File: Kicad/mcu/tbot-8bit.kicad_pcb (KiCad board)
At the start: 2 copper layers, 80 x 100 mm, 69 parts, among them IC201 TLV1117-50, IC301 PIC16F1778, IC401 MCP2221A, K201 Battery, K301 MCU 1, K302 ICSP, K303 MCU 2, K401 VIN, K402 FRONT #1, K403 +5V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

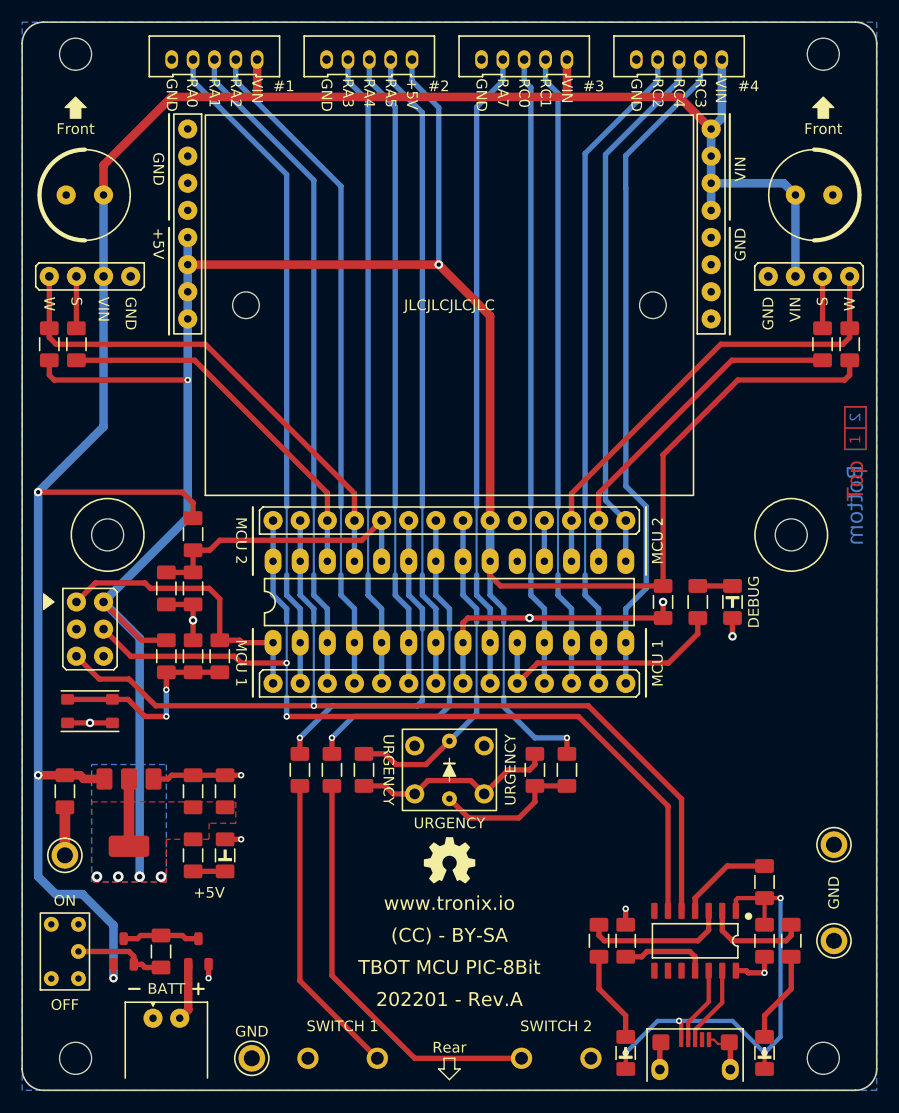
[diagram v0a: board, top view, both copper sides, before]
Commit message: Update MCU 8Bit
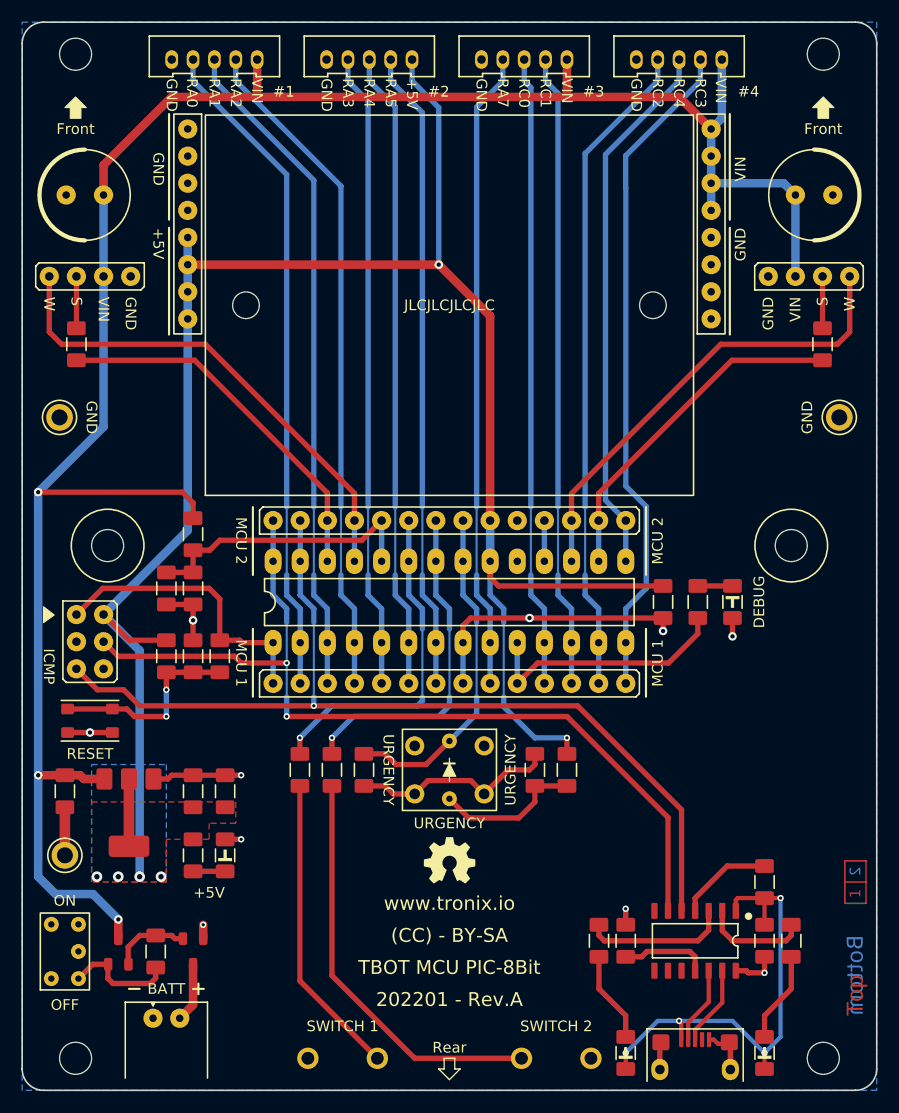
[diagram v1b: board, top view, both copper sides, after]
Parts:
- removed R407, R412: 10K, tronixio:RESISTOR-1206
- removed TP204: GND, tronixio:KEYSTONE-5006
- IC301: footprint tronixio:DIP-28-W762 -> tronixio:DIP-28-W762-SOCKET
- K401, K403: footprint tronixio:zzHARWIN-M20-782084x -> tronixio:HARWIN-M20-782084x
- K402, K404, K407, K409: footprint tronixio:zzMOLEX-532530570 -> tronixio:MOLEX-532530570
- R201: value 100K -> 1M
- S201: footprint tronixio:zzzE-SWITCH-200USPXT1A1M2RE -> tronixio:E-SWITCH-200USPXT1A1M2RE
- S401: footprint tronixio:zzzE-SWITCH-TL1240XQ1JXXX -> tronixio:E-SWITCH-TL1240XQ1JXXX
- S402, S403: footprint tronixio:zzzCK-PTS635S-TH -> tronixio:CK-PTS635S-TH
- T201, T202: footprint tronixio:zzzSOT-23-3 -> tronixio:SOT-23-3
- moved G*** 66.5 mm to (140.0, 128.5)
- moved TP203 62.6 mm to (103.5, 87.0), turned to 0 degrees
- moved TP201 40.0 mm to (176.5, 87.0)
- moved K302 1.18 mm to (105.1, 105.5)
- moved H103 1.00 mm to (172.0, 99.0)
- moved H106 1.00 mm to (108.0, 99.0)
- moved S301 0.90 mm to (106.3, 115.4)
- moved R201 0.50 mm to (112.5, 137.0)
- moved T201 0.50 mm to (116.0, 137.0), turned to -90 degrees
- moved T202 0.50 mm to (109.0, 137.0)
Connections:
- net RA0 renamed /HID/RA0
- net RA1 renamed /HID/RA1
- net RA2 renamed /HID/RA2
- net RA3 renamed /HID/RA3
- net RA4 renamed /HID/RA4
- net RA5 renamed /HID/RA5
- net RA6/LED renamed /HID/RA6/LED
- net RA7 renamed /HID/RA7
- net RB0/EMERGENCY renamed /HID/RB0/EMERGENCY
- net RB1/SWITCH_2 renamed /HID/RB1/SWITCH_2
- net RB2/SWITCH_1 renamed /HID/RB2/SWITCH_1
- net RB3/BATTERY_SENSE renamed /MCU/RB3/BATTERY_SENSE
- net RB4/WHEEL_L renamed /HID/RB4/WHEEL_L
- net RB5/SERVO_L renamed /HID/RB5/SERVO_L
- net RB6/PGC/UTX renamed /HID/RB6/PGC/UTX
- net RB7/PGD/URX renamed /HID/RB7/PGD/URX
- net RC0 renamed /HID/RC0
- net RC1 renamed /HID/RC1
- net RC2 renamed /HID/RC2
- net RC3 renamed /HID/RC3
- net RC4 renamed /HID/RC4
- net RC5/SERVO_R renamed /HID/RC5/SERVO_R
- net RC6/WHEEL_R renamed /HID/RC6/WHEEL_R
- net RC7 renamed /MCU/RC7
- S201 pad 2: Net-(R201-Pad1) -> GND
- S201 pad 3: GND -> Net-(R201-Pad1)
- T201 pad 1: VBAT -> GND
- T201 pad 2: GND -> Net-(R201-Pad2)
- T201 pad 3: Net-(R201-Pad2) -> VBAT
- T202 pad 1: VIN -> Net-(R201-Pad1)
- T202 pad 2: Net-(R201-Pad1) -> Net-(R201-Pad2)
- T202 pad 3: Net-(R201-Pad2) -> VIN
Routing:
- net +5V: track 241.1 -> 192.0 mm, vias 7 -> 6
- net VIN: track 205.3 -> 201.1 mm
- net Net-(R201-Pad1): track 8.79 -> 10.5 mm
- net /HID/RB7/PGD/URX: track 86.3 -> 85.2 mm
- net /HID/RB6/PGC/UTX: track 90.5 -> 89.5 mm
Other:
- board text added: "ICMP"
- board text added: "RESET"

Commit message: Update MCU 8Bit
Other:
- board text added: "ICSP"
- board text added: "URX"
- board text added: "UTX"
- board text removed: "ICMP"
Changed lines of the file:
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@@
   (gr_poly
     (pts
-      (xy 106 58)
+      (xy 106 57)
+      (xy 105.5 57)
       (xy 105.5 58)
-      (xy 105.5 59)
-      (xy 104.5 59)
       (xy 104.5 58)
-      (xy 104 58)
-      (xy 105 57)
+      (xy 104.5 57)
+      (xy 104 57)
+      (xy 105 56)
     ) (layer "F.SilkS") (width 0.1) (fill solid))
   (gr_line (start 116 140.5) (end 117 140.5) (layer "F.SilkS") (width 0.2))
@@
   (gr_poly
     (pts
-      (xy 176 58)
+      (xy 176 57)
+      (xy 175.5 57)
       (xy 175.5 58)
-      (xy 175.5 59)
-      (xy 174.5 59)
       (xy 174.5 58)
-      (xy 174 58)
-      (xy 175 57)
+      (xy 174.5 57)
+      (xy 174 57)
+      (xy 175 56)
     ) (layer "F.SilkS") (width 0.1) (fill solid))
   (gr_poly
@@
   )
   (gr_text "(CC) - BY-SA" (at 140 137) (layer "B.SilkS")
-    (effects (font (size 1.3 1.3) (thickness 0.15)) (justify mirror))
+    (effects (font (size 1 1) (thickness 0.15)) (justify mirror))
   )
   (gr_text "202201 - Rev.A" (at 140 144) (layer "B.SilkS")
-    (effects (font (size 1.3 1.3) (thickness 0.15)) (justify mirror))
+    (effects (font (size 1 1) (thickness 0.15)) (justify mirror))
   )
   (gr_text "TBOT MCU PIC-8Bit" (at 140 140.5) (layer "B.SilkS")
-    (effects (font (size 1.3 1.3) (thickness 0.2)) (justify mirror))
+    (effects (font (size 1 1) (thickness 0.2)) (justify mirror))
   )
   (gr_text "www.tronix.io" (at 140 133.5) (layer "B.SilkS")
-    (effects (font (size 1.3 1.3) (thickness 0.15)) (justify mirror))
+    (effects (font (size 1 1) (thickness 0.15)) (justify mirror))
   )
   (gr_text "VIN" (at 167.25 63.75 90) (layer "F.SilkS")
@@
     (effects (font (size 1 1) (thickness 0.15)))
   )
-  (gr_text "Front" (at 175 60) (layer "F.SilkS")
+  (gr_text "Front" (at 175 59) (layer "F.SilkS")
     (effects (font (size 1 1) (thickness 0.15)))
   )
   (gr_text "TBOT MCU PIC-8Bit" (at 140 138.5) (layer "F.SilkS")
-    (effects (font (size 1.3 1.3) (thickness 0.2)))
+    (effects (font (size 1 1) (thickness 0.2)))
   )
   (gr_text "MCU 2" (at 159.5 98.55 90) (layer "F.SilkS")
@@
   )
   (gr_text "SWITCH 1" (at 130 144) (layer "F.SilkS")
-    (effects (font (size 1 1) (thickness 0.15)))
+    (effects (font (size 0.8 0.8) (thickness 0.15)))
   )
   (gr_text "JLCJLCJLCJLC" (at 140 76.5) (layer "F.SilkS")
-    (effects (font (size 1 1) (thickness 0.15)))
+    (effects (font (size 0.8 0.8) (thickness 0.1)))
   )
   (gr_text "SWITCH 2" (at 150 144) (layer "F.SilkS")
-    (effects (font (size 1 1) (thickness 0.15)))
+    (effects (font (size 0.8 0.8) (thickness 0.15)))
   )
   (gr_text "W" (at 102.54 75.705 270) (layer "F.SilkS")
@@
     (effects (font (size 1 1) (thickness 0.15)))
   )
+  (gr_text "URX" (at 156.5 144 90) (layer "F.SilkS")
+    (effects (font (size 0.8 0.8) (thickness 0.15)) (justify left))
+  )
   (gr_text "GND" (at 110.16 75.705 270) (layer "F.SilkS")
     (effects (font (size 1 1) (thickness 0.15)) (justify left))
   )
   (gr_text "GND" (at 128.5 55.25 270) (layer "F.SilkS")
-    (effects (font (size 1 1) (thickness 0.15)) (justify left))
+    (effects (font (size 0.8 0.8) (thickness 0.15)) (justify left))
   )
   (gr_text "ON" (at 104 132.25) (layer "F.SilkS")
@@
   )
   (gr_text "RA1" (at 118 55.25 270) (layer "F.SilkS")
-    (effects (font (size 1 1) (thickness 0.15)) (justify left))
+    (effects (font (size 0.8 0.8) (thickness 0.15)) (justify left))
   )
   (gr_text "#3" (at 153.5 56.5) (layer "F.SilkS")
@@
   )
   (gr_text "RA4" (at 132.5 55.25 270) (layer "F.SilkS")
-    (effects (font (size 1 1) (thickness 0.15)) (justify left))
+    (effects (font (size 0.8 0.8) (thickness 0.15)) (justify left))
   )
   (gr_text "www.tronix.io" (at 140 132.5) (layer "F.SilkS")
-    (effects (font (size 1.3 1.3) (thickness 0.15)))
+    (effects (font (size 1 1) (thickness 0.15)))
   )
   (gr_text "RA0" (at 115.9 55.25 270) (layer "F.SilkS")
-    (effects (font (size 1 1) (thickness 0.15)) (justify left))
+    (effects (font (size 0.8 0.8) (thickness 0.15)) (justify left))
   )
   (gr_text "VIN" (at 172.39 75.705 90) (layer "F.SilkS")
     (effects (font (size 1 1) (thickness 0.15)) (justify right))
   )
-  (gr_text "ICMP" (at 102.5 112 270) (layer "F.SilkS")
-    (effects (font (size 1 1) (thickness 0.15)) (justify right))
+  (gr_text "ICSP" (at 102.5 112 270) (layer "F.SilkS")
+    (effects (font (size 1 1) (thickness 0.15)) (justify right))
+  )
+  (gr_text "UTX" (at 169.5 144 90) (layer "F.SilkS")
+    (effects (font (size 0.8 0.8) (thickness 0.15)) (justify left))
   )
   (gr_text "URGENCY" (at 140 125) (layer "F.SilkS")
-    (effects (font (size 1 1) (thickness 0.15)))
+    (effects (font (size 0.8 0.8) (thickness 0.15)))
   )
   (gr_text "RA2" (at 120 55.25 270) (layer "F.SilkS")
-    (effects (font (size 1 1) (thickness 0.15)) (justify left))
+    (effects (font (size 0.8 0.8) (thickness 0.15)) (justify left))
   )
   (gr_text "VIN" (at 107.62 75.705 270) (layer "F.SilkS")
@@
   )
   (gr_text "RC2" (at 159.5 55.25 270) (layer "F.SilkS")
-    (effects (font (size 1 1) (thickness 0.15)) (justify left))
+    (effects (font (size 0.8 0.8) (thickness 0.15)) (justify left))
   )
   (gr_text "202201 - Rev.A" (at 140 141.5) (layer "F.SilkS")
-    (effects (font (size 1.3 1.3) (thickness 0.15)))
+    (effects (font (size 1 1) (thickness 0.15)))
   )
   (gr_text "GND" (at 143 55.25 270) (layer "F.SilkS")
-    (effects (font (size 1 1) (thickness 0.15)) (justify left))
+    (effects (font (size 0.8 0.8) (thickness 0.15)) (justify left))
   )
   (gr_text "GND" (at 169.85 75.705 90) (layer "F.SilkS")
@@
   )
   (gr_text "RA3" (at 130.5 55.25 270) (layer "F.SilkS")
-    (effects (font (size 1 1) (thickness 0.15)) (justify left))
+    (effects (font (size 0.8 0.8) (thickness 0.15)) (justify left))
   )
   (gr_text "RC4" (at 161.5 55.25 270) (layer "F.SilkS")
-    (effects (font (size 1 1) (thickness 0.15)) (justify left))
+    (effects (font (size 0.8 0.8) (thickness 0.15)) (justify left))
   )
   (gr_text "RA5" (at 134.5 55.25 270) (layer "F.SilkS")
-    (effects (font (size 1 1) (thickness 0.15)) (justify left))
+    (effects (font (size 0.8 0.8) (thickness 0.15)) (justify left))
   )
   (gr_text "GND" (at 114 55.25 270) (layer "F.SilkS")
-    (effects (font (size 1 1) (thickness 0.15)) (justify left))
+    (effects (font (size 0.8 0.8) (thickness 0.15)) (justify left))
   )
   (gr_text "URGENCY" (at 134.29 120 270) (layer "F.SilkS")
-    (effects (font (size 1 1) (thickness 0.15)))
+    (effects (font (size 0.8 0.8) (thickness 0.15)))
   )
   (gr_text "MCU 1" (at 120.5 110 270) (layer "F.SilkS")
@@
   )
   (gr_text "VIN" (at 151 55.25 270) (layer "F.SilkS")
-    (effects (font (size 1 1) (thickness 0.15)) (justify left))
+    (effects (font (size 0.8 0.8) (thickness 0.15)) (justify left))
   )
   (gr_text "#2" (at 139 56.5) (layer "F.SilkS")
@@
   )
   (gr_text "VIN" (at 165.4 55.25 270) (layer "F.SilkS")
-    (effects (font (size 1 1) (thickness 0.15)) (justify left))
+    (effects (font (size 0.8 0.8) (thickness 0.15)) (justify left))
   )
   (gr_text "+5V" (at 136.5 55.25 270) (layer "F.SilkS")
-    (effects (font (size 1 1) (thickness 0.15)) (justify left))
+    (effects (font (size 0.8 0.8) (thickness 0.15)) (justify left))
   )
   (gr_text "+5V" (at 117.5 131.5) (layer "F.SilkS")
     (effects (font (size 1 1) (thickness 0.15)))
   )
-  (gr_text "Front" (at 105 60) (layer "F.SilkS")
+  (gr_text "Front" (at 105 59) (layer "F.SilkS")
     (effects (font (size 1 1) (thickness 0.15)))
   )
@@
   )
   (gr_text "VIN" (at 122 55.25 270) (layer "F.SilkS")
-    (effects (font (size 1 1) (thickness 0.15)) (justify left))
+    (effects (font (size 0.8 0.8) (thickness 0.15)) (justify left))
   )
   (gr_text "+5V" (at 112.75 69.25 270) (layer "F.SilkS")
@@
   )
   (gr_text "URGENCY" (at 145.72 120 90) (layer "F.SilkS")
-    (effects (font (size 1 1) (thickness 0.15)))
+    (effects (font (size 0.8 0.8) (thickness 0.15)))
   )
   (gr_text "(CC) - BY-SA" (at 140 135.5) (layer "F.SilkS")
-    (effects (font (size 1.3 1.3) (thickness 0.15)))
+    (effects (font (size 1 1) (thickness 0.15)))
   )
   (gr_text "RC1" (at 149 55.25 270) (layer "F.SilkS")
-    (effects (font (size 1 1) (thickness 0.15)) (justify left))
+    (effects (font (size 0.8 0.8) (thickness 0.15)) (justify left))
   )
   (gr_text "BATT" (at 113.5 140.5) (layer "F.SilkS")
@@
   )
   (gr_text "GND" (at 157.5 55.25 270) (layer "F.SilkS")
-    (effects (font (size 1 1) (thickness 0.15)) (justify left))
+    (effects (font (size 0.8 0.8) (thickness 0.15)) (justify left))
   )
   (gr_text "RC3" (at 163.5 55.25 270) (layer "F.SilkS")
-    (effects (font (size 1 1) (thickness 0.15)) (justify left))
+    (effects (font (size 0.8 0.8) (thickness 0.15)) (justify left))
   )
   (gr_text "RA7" (at 145 55.25 270) (layer "F.SilkS")
-    (effects (font (size 1 1) (thickness 0.15)) (justify left))
+    (effects (font (size 0.8 0.8) (thickness 0.15)) (justify left))
   )
   (gr_text "RC0" (at 147 55.25 270) (layer "F.SilkS")
-    (effects (font (size 1 1) (thickness 0.15)) (justify left))
+    (effects (font (size 0.8 0.8) (thickness 0.15)) (justify left))
   )
   (gr_text "TBOT MCU PIC-8Bit - Rev.A - (01/2022) - Scale 100%" (at 100 160) (layer "Dwgs.User")

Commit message: Update MCU
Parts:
- removed K409: FRONT #4, tronixio:MOLEX-532530570
- removed R410, R411: 5K6, tronixio:RESISTOR-1206
- removed R413: 220Ω, tronixio:RESISTOR-1206
- removed S402: Switch 1, tronixio:CK-PTS635S-TH
- removed S403: Switch 2, tronixio:CK-PTS635S-TH
- added R407: 4K7, tronixio:RESISTOR-1206, F.Cu at (154.0, 136.0)
- K401: value VIN -> FRONT #1; footprint tronixio:HARWIN-M20-782084x -> tronixio:MOLEX-532530570
- K402: value FRONT #1 -> FRONT #2
- K403: value +5V -> VIN
- K404: value FRONT #2 -> +5V; footprint tronixio:MOLEX-532530570 -> tronixio:HARWIN-M20-782084x
- K405: value SERVO LEFT -> FRONT #3; footprint tronixio:HARWIN-M20-999044x -> tronixio:MOLEX-532530570
- K406: value USB/UART -> SERVO LEFT; footprint tronixio:FCI-USB-TYPE-B-MICRO-THT -> tronixio:HARWIN-M20-999044x
- K407: value FRONT #3 -> USB/UART; footprint tronixio:MOLEX-532530570 -> tronixio:FCI-USB-TYPE-B-MICRO-THT
- R401: value 4K7 -> 220Ω
- R402: value 220Ω -> 150Ω
- R403: value 150Ω -> 330Ω
- R404: value 330Ω -> 4K7
- R405: value 1K -> 220Ω
- R406: value 1K -> 10K
- R409: value 10K -> 4K7
- moved K407 96.1 mm to (163.0, 147.5), turned to 90 degrees
- moved K406 90.7 mm to (110.2, 73.8), turned to -90 degrees
- moved R408 69.9 mm to (174.9, 80.2)
- moved K403 52.1 mm to (164.5, 60.0), turned to 0 degrees
- moved R406 48.2 mm to (174.5, 136.0), turned to -90 degrees
- moved K405 46.5 mm to (152.0, 53.5), turned to 0 degrees
- moved R405 45.0 mm to (105.1, 80.2)
- moved K401 45.0 mm to (120.0, 53.5)
- moved R404 35.0 mm to (163.2, 104.3), turned to -90 degrees
- moved K404 27.5 mm to (115.5, 77.8), turned to 180 degrees
- moved K402 22.0 mm to (136.0, 53.5)
- moved R401 19.9 mm to (151.0, 120.0), turned to 90 degrees
- moved R403 16.2 mm to (131.8, 120.0), turned to 90 degrees
- moved R409 6.04 mm to (172.0, 136.0)
- moved R402 3.00 mm to (148.0, 120.0), turned to -90 degrees
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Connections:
- net /HID/RC3 renamed RC3
- net /HID/RC4 renamed RC4
- net /MCU/RC7 renamed RC7
- IC301 pad 22: /HID/RB1/SWITCH_2 -> RB1
- IC301 pad 23: /HID/RB2/SWITCH_1 -> RB2
- IC301 pad 9: /HID/RA7 -> RA7
- K301 pad 9: /HID/RA7 -> RA7
- K303 pad 6: /HID/RB2/SWITCH_1 -> RB2
- K303 pad 7: /HID/RB1/SWITCH_2 -> RB1
- K401 pad 2: VIN -> /HID/RA2
- K401 pad 3: VIN -> /HID/RA1
- K401 pad 4: VIN -> /HID/RA0
- K402 pad 1: VIN -> +5V
- K402 pad 2: /HID/RA2 -> /HID/RA5
- K402 pad 3: /HID/RA1 -> /HID/RA4
- K402 pad 4: /HID/RA0 -> /HID/RA3
- K403 pad 1: +5V -> VIN
- K403 pad 2: +5V -> VIN
- K403 pad 3: +5V -> VIN
- K403 pad 4: +5V -> VIN
- K404 pad 2: /HID/RA5 -> +5V
- K404 pad 3: /HID/RA4 -> +5V
- K404 pad 4: /HID/RA3 -> +5V
- K405 pad 1: GND -> VIN
- K405 pad 2: VIN -> /HID/RC2
- K405 pad 3: Net-(K405-Pad3) -> /HID/RC1
- K405 pad 4: /HID/RB4/WHEEL_L -> /HID/RC0
- K406 pad 1: VUSB -> GND
- K406 pad 2: /HID/D- -> VIN
- K406 pad 3: /HID/D+ -> Net-(K406-Pad3)
- K406 pad 4: unconnected-(K406-Pad4) -> /HID/RB4/WHEEL_L
- K407 pad 1: VIN -> VUSB
- K407 pad 2: /HID/RC1 -> /HID/D-
- K407 pad 3: /HID/RC0 -> /HID/D+
- K407 pad 4: /HID/RA7 -> unconnected-(K407-Pad4)
- R401 pad 1: Net-(LED401-Pad2) -> Net-(R401-Pad1)
- R401 pad 2: /HID/RA6/LED -> +5V
- R402 pad 2: +5V -> Net-(R401-Pad1)
- R403 pad 1: Net-(R403-Pad1) -> Net-(R402-Pad1)
- R403 pad 2: Net-(R402-Pad1) -> /HID/RB0/EMERGENCY
- R404 pad 1: Net-(R403-Pad1) -> Net-(LED401-Pad2)
- R404 pad 2: /HID/RB0/EMERGENCY -> /HID/RA6/LED
- R405 pad 1: Net-(R405-Pad1) -> /HID/RB5/SERVO_L
- R405 pad 2: /HID/RB2/SWITCH_1 -> Net-(K406-Pad3)
- R406 pad 1: Net-(R406-Pad1) -> Net-(IC401-Pad4)
- R406 pad 2: /HID/RB1/SWITCH_2 -> VUSB
- R408 pad 1: /HID/RB5/SERVO_L -> /HID/RC5/SERVO_R
- R408 pad 2: Net-(K405-Pad3) -> Net-(K408-Pad3)
- R409 pad 1: Net-(IC401-Pad4) -> Net-(IC401-Pad2)
- R409 pad 2: VUSB -> Net-(LED403-Pad1)
- S401 pad 3: Net-(R403-Pad1) -> Net-(R402-Pad1)
- S401 pad 4: Net-(R403-Pad1) -> Net-(R402-Pad1)
- S401 pad 6: Net-(R402-Pad1) -> Net-(R401-Pad1)
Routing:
- net /HID/RA7: track 59.9 -> 0.00 mm
- net RC3: track 62.8 -> 3.81 mm
- net RC4: track 50.6 -> 3.81 mm
- net Net-(R406-Pad1): track 38.7 -> 0.00 mm
- net /HID/RB2/SWITCH_1: track 31.8 -> 0.00 mm, vias 1 -> 0
- net /HID/RB1/SWITCH_2: track 31.6 -> 0.00 mm, vias 1 -> 0
- net Net-(R405-Pad1): track 28.5 -> 0.00 mm
- net Net-(R403-Pad1): track 19.5 -> 0.00 mm
- net Net-(R401-Pad1): track 0.00 -> 13.9 mm
- net Net-(IC401-Pad4): track 8.94 -> 16.3 mm
- net Net-(R402-Pad1): track 13.9 -> 19.5 mm
- net VIN: track 201.1 -> 195.9 mm
- net Net-(K406-Pad3): track 0.00 -> 4.85 mm
- net Net-(K405-Pad3): track 4.85 -> 0.00 mm
- net RB2: track 0.00 -> 3.81 mm
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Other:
- board text added: "DATA"
- board text removed: "#4"
- board text removed: "RA7"
- board text removed: "RC3"
- board text removed: "RC4"
- board text removed: "SWITCH 1"
- board text removed: "SWITCH 2"
